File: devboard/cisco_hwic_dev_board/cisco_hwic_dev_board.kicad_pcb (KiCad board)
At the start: 2 copper layers, 31 x 52.1 mm, 17 parts, among them J1 Conn_02x20_Odd_Even, J2 Conn_02x34_Top_Bottom_Cisco, J3 Conn_01x15, J4 USB Blaster Active Serial, J5 ATT85_VIN, J6 SD Card, J7 Power, U1 AT25xxx, U2 ATtiny85_devboard

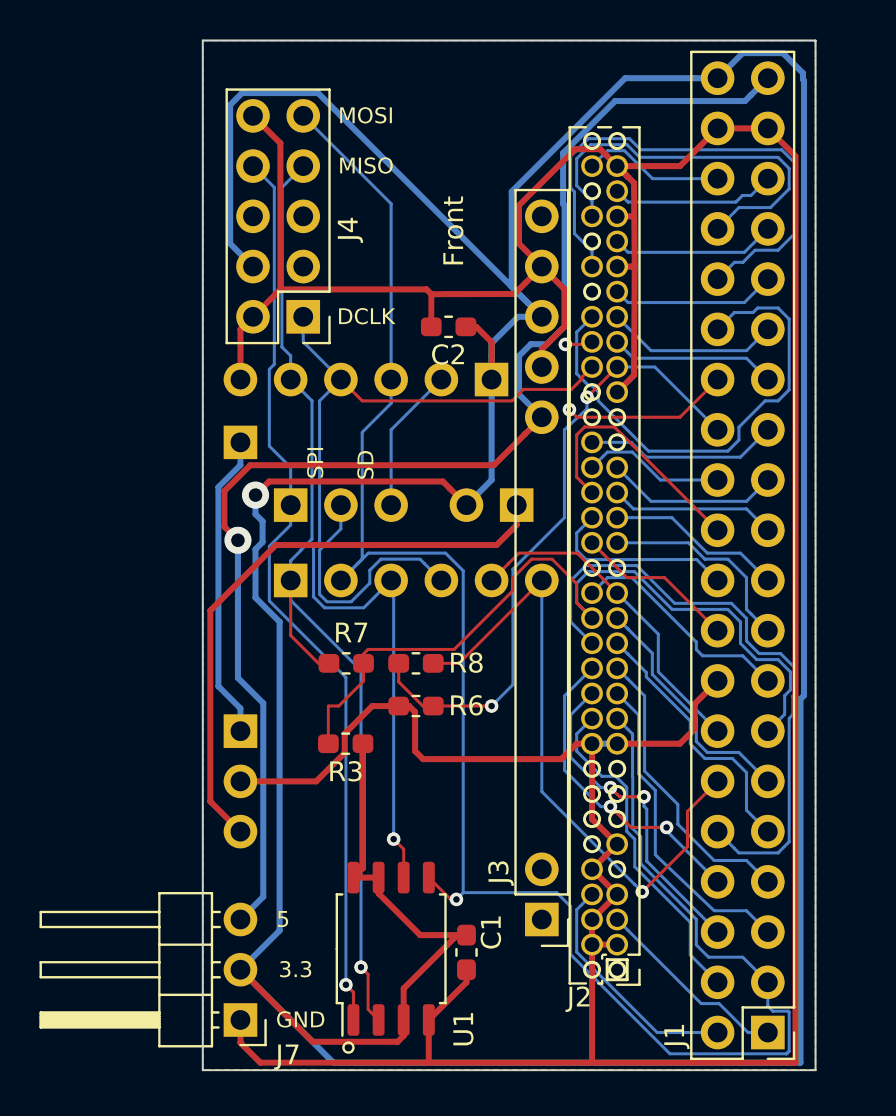
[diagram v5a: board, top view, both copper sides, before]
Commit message: Change 2x34 connector footprint. Increase distance to HWIC connector.
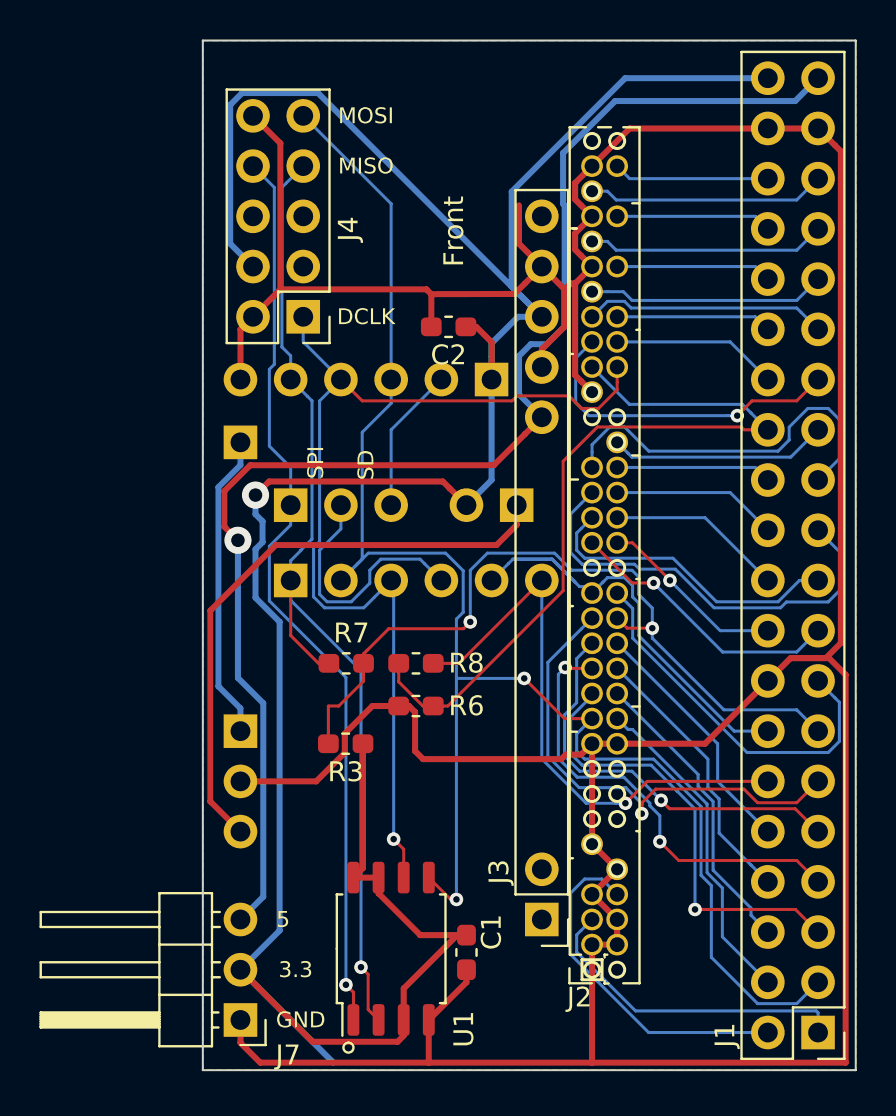
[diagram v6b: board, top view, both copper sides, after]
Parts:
- moved J1 2.54 mm to (-527.7, -536.6)
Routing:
- net +3V3: track 218.1 -> 141.6 mm
- net /PG5: track 26.7 -> 7.88 mm
- net /PB7: track 31.4 -> 12.7 mm
- net /PG3: track 25.4 -> 7.88 mm
- net /PD4: track 8.41 -> 22.2 mm
- net /PB8: track 12.3 -> 24.7 mm, vias 0 -> 1
- net /PG7: track 20.3 -> 7.88 mm
- net /DATA0: track 95.5 -> 83.9 mm, vias 1 -> 2
- net /PD6: track 8.78 -> 19.6 mm
- net /PG0: track 8.41 -> 16.9 mm, vias 0 -> 1
- net /PB4: track 14.9 -> 22.7 mm, vias 0 -> 2
- net /DCLK_ALT: track 32.3 -> 40.1 mm, vias 2 -> 0
- net /PC2: track 11.6 -> 19.2 mm
- net /PB6: track 13.5 -> 20.7 mm, vias 0 -> 1
- net GND: track 203.2 -> 210.2 mm
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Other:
- board size 31 x 52.1 mm -> 33 x 52.1 mm
- board text added: "3V3"
- board text added: "AT_PB5"
- board text added: "PA1"
- board text added: "PB1"
- board text added: "PB3"
- board text added: "PB5"
- board text added: "PB7"
- board text added: "PC1"
- board text added: "PD1"
- board text added: "PD3"
- board text added: "PD5"
- board text added: "PD7"
- board text added: "PE1"
- board text added: "PG1"
- board text added: "PG3"
- board text added: "PG5"
- board text added: "PG7"
- board text added: "PH1"
